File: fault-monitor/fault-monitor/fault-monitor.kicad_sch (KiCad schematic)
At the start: 15 parts, among them U1 ESP32-DevKitC, U2 DS18B20T(XBLW)

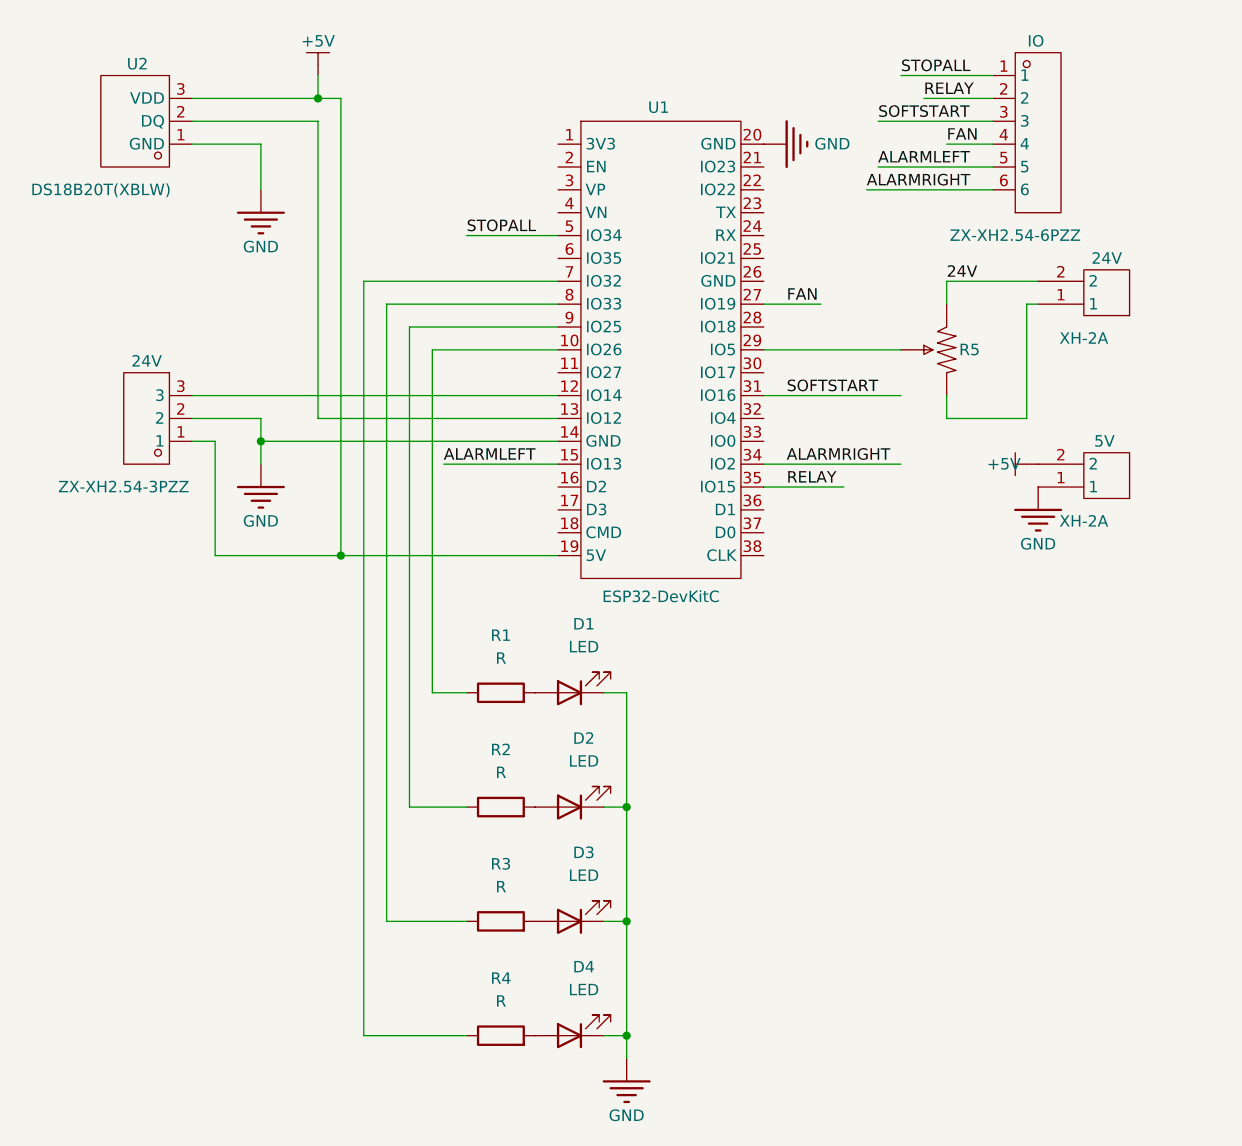
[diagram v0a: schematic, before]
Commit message: replace current sensor connector and power labels
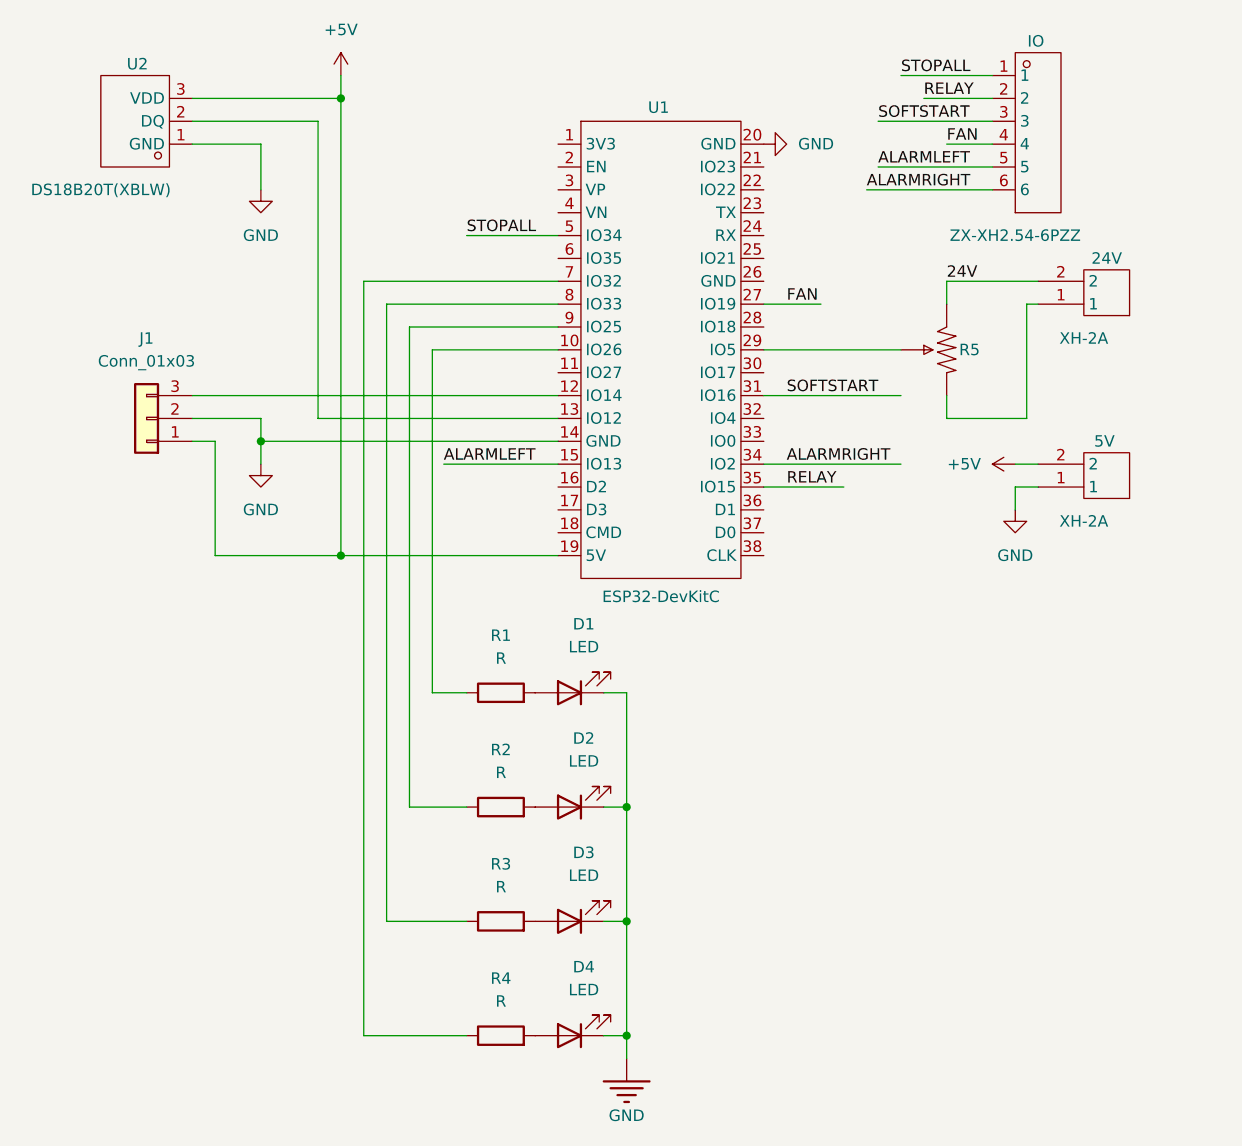
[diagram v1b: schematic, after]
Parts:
- removed 24V: ZX-XH2.54-3PZZ, ProPrj_Fau-easyedapro:CONN-TH_3P-P2.54_2501S-3P, symbol ProPrj_Fau-easyedapro:ZX-XH2.54-3PZZ
- added J1: Conn_01x03, symbol Connector_Generic:Conn_01x03
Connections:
- net +5V: now also J1.1 (Pin_1)
- net GND: now also J1.2 (Pin_2)
- net at U1.12 (IO14): now also J1.3 (Pin_3)

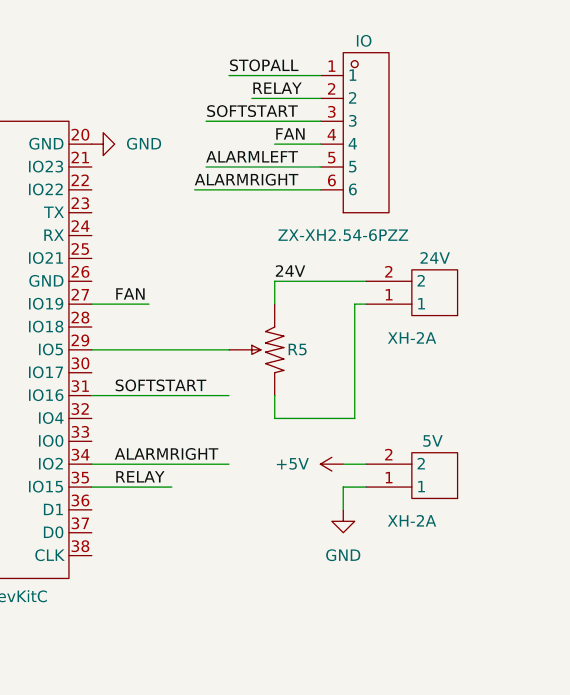
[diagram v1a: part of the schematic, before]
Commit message: update connectors
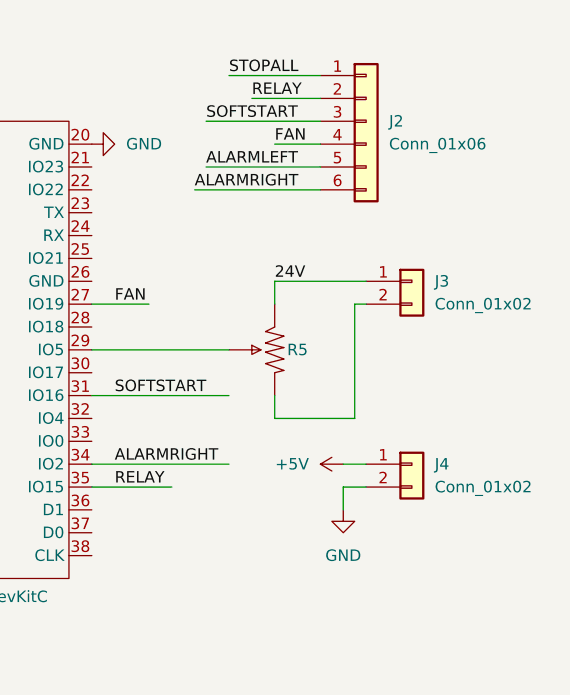
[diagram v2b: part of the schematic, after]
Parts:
- removed 24V, 5V: XH-2A, ProPrj_Fau-easyedapro:CONN-TH_XH-2A, symbol ProPrj_Fau-easyedapro:XH-2A
- removed IO: ZX-XH2.54-6PZZ, ProPrj_Fau-easyedapro:CONN-TH_6P-P2.50_ZX-XH2.54-6PZZ, symbol ProPrj_Fau-easyedapro:ZX-XH2.54-6PZZ
- added J2: Conn_01x06, symbol Connector_Generic:Conn_01x06
- added J3, J4: Conn_01x02, symbol Connector_Generic:Conn_01x02
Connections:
- net +5V: now also J4.1 (Pin_1)
- net 24V: now also J3.1 (Pin_1)
- net ALARMLEFT: now also J2.5 (Pin_5)
- net ALARMRIGHT: now also J2.6 (Pin_6)
- net FAN: now also J2.4 (Pin_4)
- net GND: now also J4.2 (Pin_2)
- net RELAY: now also J2.2 (Pin_2)
- net SOFTSTART: now also J2.3 (Pin_3)
- net STOPALL: now also J2.1 (Pin_1)
- net at R5.1: now also J3.2 (Pin_2)

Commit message: replace pot
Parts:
- removed R5: 10kΩ, ProPrj_Fau-easyedapro:RES-ADJ-TH_3362P, symbol ProPrj_Fau-easyedapro:3362P-103-3H
- added RV1: R_Potentiometer, symbol Device:R_Potentiometer
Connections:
- net 24V: now also RV1.3
- net at J3.2 (Pin_2): now also RV1.1
- net at U1.29 (IO5): now also RV1.2
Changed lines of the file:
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@@
 	(wire
 		(pts
-			(xy 95.25 50.8) (xy 110.49 50.8)
+			(xy 95.25 50.8) (xy 111.76 50.8)
 		)
 		(stroke
@@
 	(wire
 		(pts
-			(xy 115.57 43.18) (xy 115.57 45.72)
-		)
-		(stroke
-			(width 0)
-			(type default)
-		)
-	)
-	(wire
-		(pts
 			(xy 124.46 58.42) (xy 124.46 45.72)
 		)
@@
 	(wire
 		(pts
-			(xy 115.57 58.42) (xy 115.57 55.88)
-		)
-		(stroke
-			(width 0)
-			(type default)
-		)
-	)
-	(wire
-		(pts
 			(xy 125.73 66.04) (xy 123.19 66.04)
 		)
@@
 	(wire
 		(pts
+			(xy 115.57 43.18) (xy 115.57 46.99)
+		)
+		(stroke
+			(width 0)
+			(type default)
+		)
+	)
+	(wire
+		(pts
 			(xy 123.19 66.04) (xy 123.19 68.58)
 		)
@@
 		(pts
 			(xy 120.65 30.48) (xy 107.95 30.48)
+		)
+		(stroke
+			(width 0)
+			(type default)
+		)
+	)
+	(wire
+		(pts
+			(xy 115.57 54.61) (xy 115.57 58.42)
 		)
 		(stroke
@@
 			)
 			(justify left bottom)
-		)
-	)
-	(symbol
-		(lib_id "ProPrj_Fau-easyedapro:3362P-103-3H")
-		(at 115.57 50.8 90)
-		(unit 1)
-		(exclude_from_sim no)
-		(in_bom yes)
-		(on_board yes)
-		(dnp no)
-		(property "Reference" "R5"
-			(at 118.11 50.8 90)
-			(effects
-				(font
-					(size 1.27 1.27)
-				)
-			)
-		)
-		(property "Value" "10kΩ"
-			(at 118.11 53.34 90)
-			(effects
-				(font
-					(size 1.27 1.27)
-				)
-				(hide yes)
-			)
-		)
-		(property "Footprint" "ProPrj_Fau-easyedapro:RES-ADJ-TH_3362P"
-			(at 115.57 50.8 0)
-			(effects
-				(font
-					(size 1.27 1.27)
-				)
-				(hide yes)
-			)
-		)
-		(property "Datasheet" "https://item.szlcsc.com/datasheet/3362P-103-3H/50920314.html"
-			(at 115.57 50.8 0)
-			(effects
-				(font
-					(size 1.27 1.27)
-				)
-				(hide yes)
-			)
-		)
-		(property "Description" "Resistance:10kΩ Tolerance:±10% Tolerance:±10% Power(Watts):500mW Temperature Coefficient:±250ppm/°C Temperature Coefficient:±250ppm/°C Number of Turns:"
-			(at 115.57 50.8 0)
-			(effects
-				(font
-					(size 1.27 1.27)
-				)
-				(hide yes)
-			)
-		)
-		(property "Manufacturer Part" "3362P-103-3H"
-			(at 115.57 50.8 0)
-			(effects
-				(font
-					(size 1.27 1.27)
-				)
-				(hide yes)
-			)
-		)
-		(property "Manufacturer" "BAOTER(宝特)"
-			(at 115.57 50.8 0)
-			(effects
-				(font
-					(size 1.27 1.27)
-				)
-				(hide yes)
-			)
-		)
-		(property "Supplier Part" "C48642051"
-			(at 115.57 50.8 0)
-			(effects
-				(font
-					(size 1.27 1.27)
-				)
-				(hide yes)
-			)
-		)
-		(property "Supplier" "LCSC"
-			(at 115.57 50.8 0)
-			(effects
-				(font
-					(size 1.27 1.27)
-				)
-				(hide yes)
-			)
-		)
-		(property "LCSC Part Name" "3362P 10KΩ±10% 高精度 高可靠 高稳定"
-			(at 115.57 50.8 0)
-			(effects
-				(font
-					(size 1.27 1.27)
-				)
-				(hide yes)
-			)
-		)
-		(pin "1"
-		)
-		(pin "2"
-		)
-		(pin "3"
-		)
-		(instances
-			(project ""
-				(path "/64884559-cbe4-442b-837a-f1967fbf7136"
-					(reference "R5")
-					(unit 1)
-				)
-			)
 		)
 	)
@@
 					(unit 1)
 				)
+			)
+		)
+	)
+	(symbol
+		(lib_id "Device:R_Potentiometer")
+		(at 115.57 50.8 180)
+		(unit 1)
+		(exclude_from_sim no)
+		(in_bom yes)
+		(on_board yes)
+		(dnp no)
+		(fields_autoplaced yes)
+		(property "Reference" "RV1"
+			(at 118.11 49.5299 0)
+			(effects
+				(font
+					(size 1.27 1.27)
+				)
+				(justify right)
+			)
+		)
+		(property "Value" "R_Potentiometer"
+			(at 118.11 52.0699 0)
+			(effects
+				(font
+					(size 1.27 1.27)
+				)
+				(justify right)
+			)
+		)
+		(property "Footprint" ""
+			(at 115.57 50.8 0)
+			(effects
+				(font
+					(size 1.27 1.27)
+				)
+				(hide yes)
+			)
+		)
+		(property "Datasheet" "~"
+			(at 115.57 50.8 0)
+			(effects
+				(font
+					(size 1.27 1.27)
+				)
+				(hide yes)
+			)
+		)
+		(property "Description" "Potentiometer"
+			(at 115.57 50.8 0)
+			(effects
+				(font
+					(size 1.27 1.27)
+				)
+				(hide yes)
+			)
+		)
+		(pin "2"
+		)
+		(pin "1"
+		)
+		(pin "3"
+		)
+		(instances
+			(project ""
+				(path "/64884559-cbe4-442b-837a-f1967fbf7136"
+					(reference "RV1")
+					(unit 1)
+				)

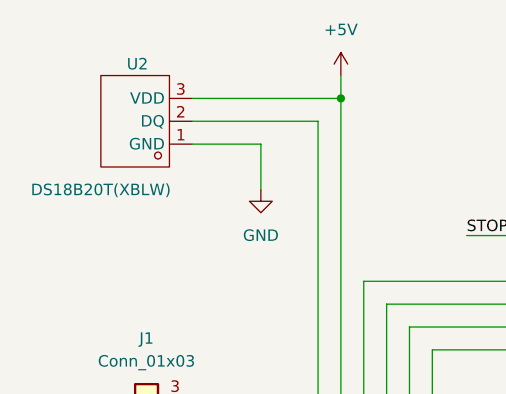
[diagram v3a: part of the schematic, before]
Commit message: replace temp sensor
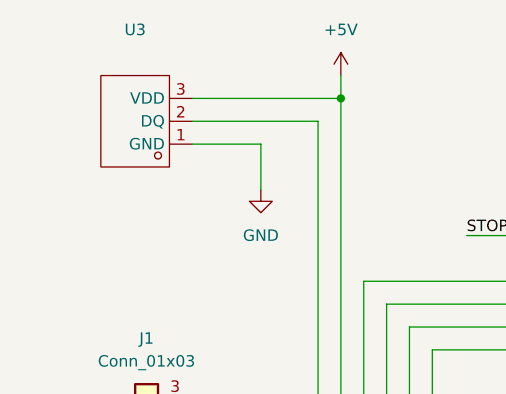
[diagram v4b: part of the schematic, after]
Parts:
- removed U2: DS18B20T(XBLW), ProPrj_Fau-easyedapro:TO-92-3_L4.5-W3.5-P1.27-L, symbol ProPrj_Fau-easyedapro:DS18B20T(XBLW)
- added U3: ~, ProPrj_Fau-easyedapro:TO-92-3_L4.5-W3.5-P1.27-L, symbol ProPrj_Fau-easyedapro:DS18B20T(XBLW)
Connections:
- net +5V: now also U3.3 (VDD)
- net GND: now also U3.1 (GND)
- net at U1.13 (IO12): now also U3.2 (DQ)
